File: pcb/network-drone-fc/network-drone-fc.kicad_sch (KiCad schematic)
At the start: 80 parts, among them J1 U.FL-R-SMT-1, J2 TYPE-C 16PIN 2MD, J3 U.FL GPS, J4 ESC, J5 Sensor port 5V I2C, J6 Radio UART 5V, J7 Charging board, U1 ESP32-S3FN8, U2 USBLC6-2SC6, U3 AP63205WU-7, U4 TLV75733PDRVR, U5 TPS7A2033PDBVR, U6 ICM-42688-P, U7 BMP581, U8 MAX-M10S, X1 Q22FA12800101

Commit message: Schematic: C16 footprint field set to 1206 to match the board
The board has carried the 1206 since the capacitor was enlarged; the schematic's footprint field still named the 0805. No copper change.
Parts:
- C16: footprint Capacitor_SMD:C_0805_2012Metric -> Capacitor_SMD:C_1206_3216Metric
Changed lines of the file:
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@@
 			)
 		)
-		(property "Footprint" "Capacitor_SMD:C_0805_2012Metric"
+		(property "Footprint" "Capacitor_SMD:C_1206_3216Metric"
 			(at 138.1252 50.8 0)
 			(effects

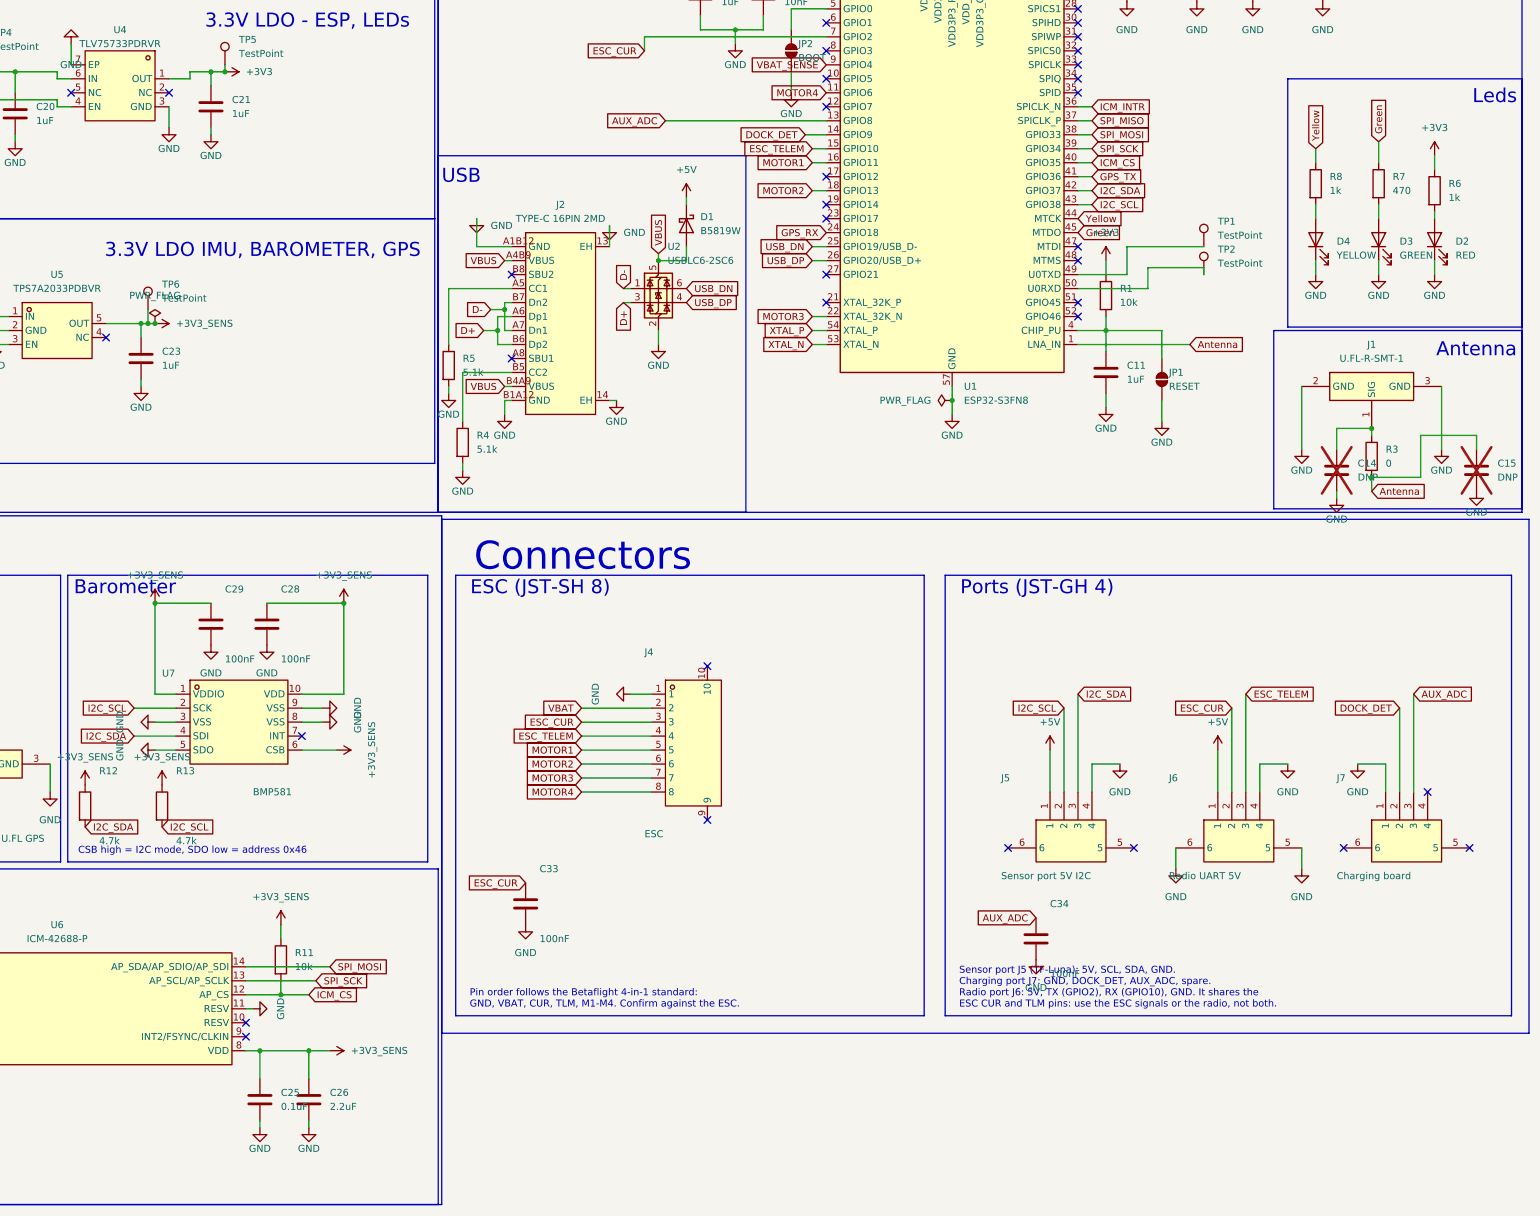
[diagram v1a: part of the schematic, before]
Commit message: Schematic: charging port J7 grows to 7 pins (battery, GND, I2C, power good, charge status, charge disable); landing sensor port J8 added; I2C pull-ups to 2.2k
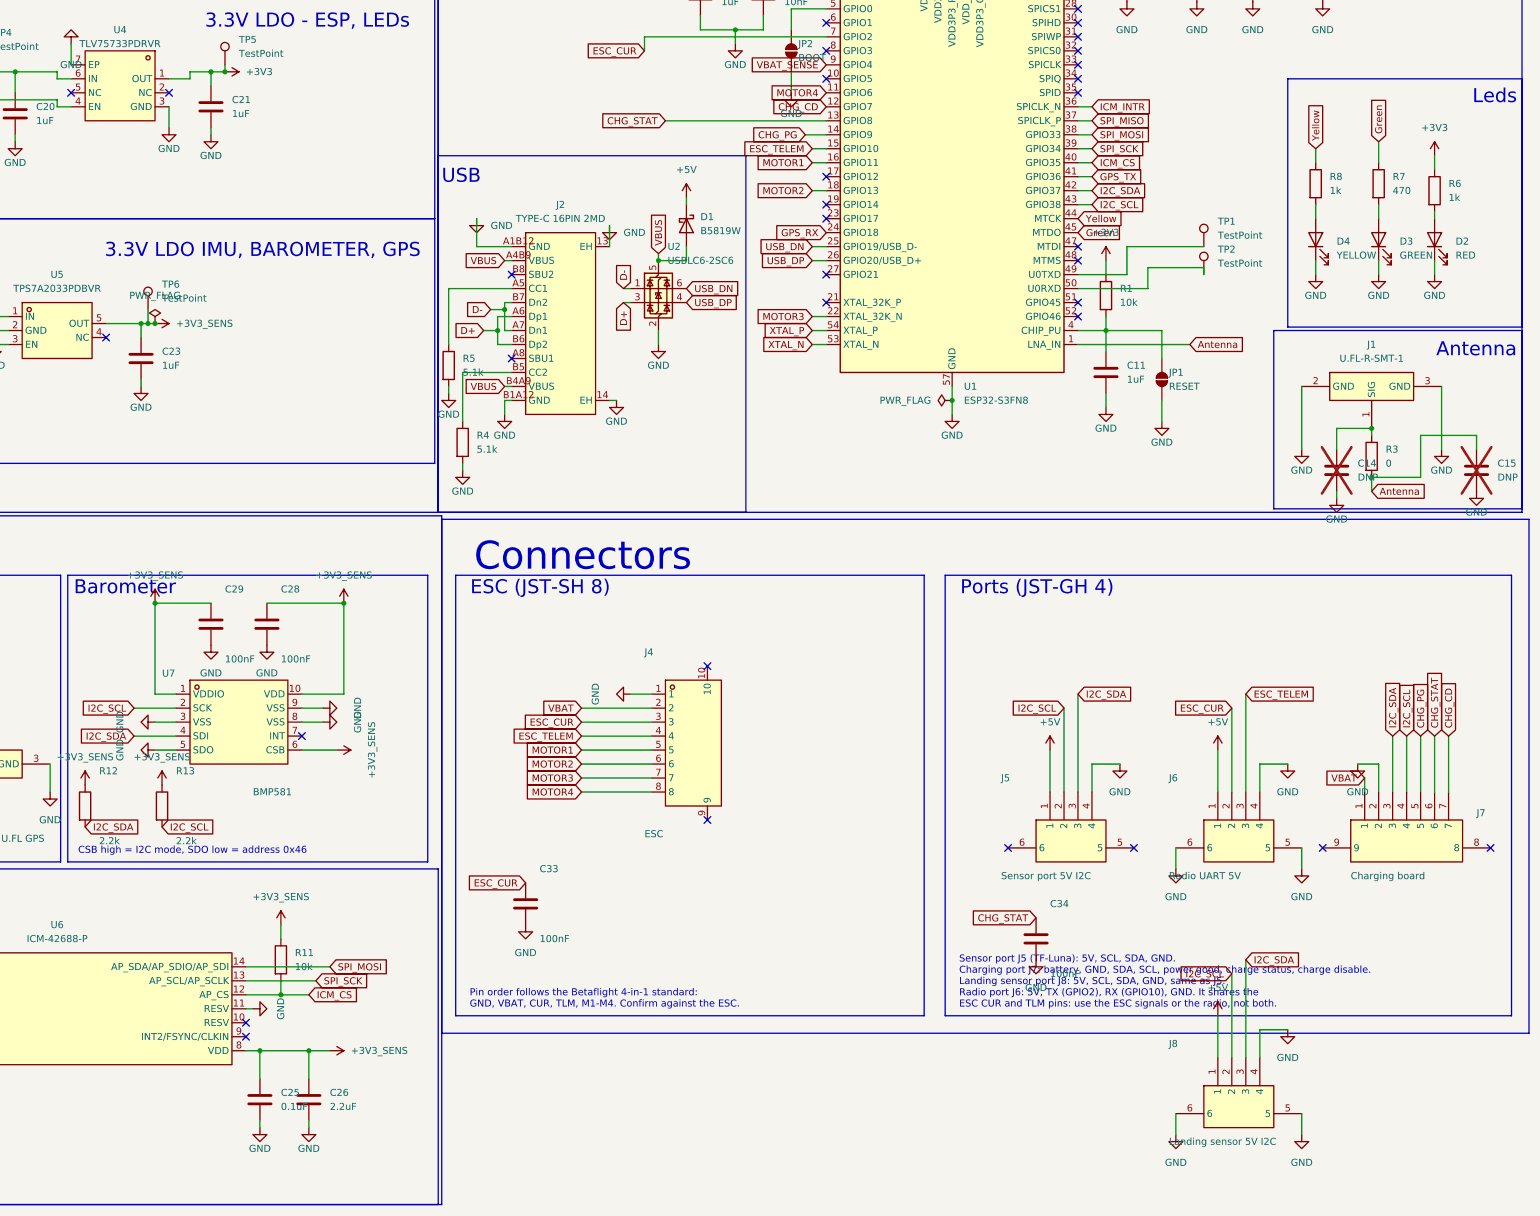
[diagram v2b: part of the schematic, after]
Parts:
- added J8: Landing sensor 5V I2C, tar_fc:JST_SH_BM04B-SRSS-TB_1x04_Vertical, symbol tar_fc:SM04B-GHS-TB
- J7: footprint tar_fc:CONN-SMD_4P-P1.25_SM04B-GHS-TB-LF-SN -> tar_fc:JST_SH_SM07B-SRSS-TB_1x07_Horizontal; symbol tar_fc:SM04B-GHS-TB -> tar_fc:SM07B-SRSS-TB; LCSC C189895 -> (none)
- R12, R13: value 4.7k -> 2.2k
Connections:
- net +5V: now also J8.1
- net GND: now also J7.2, J8.4, J8.5, J8.6; no longer J7.1
- net I2C_SCL: now also J7.4, J8.2
- net I2C_SDA: now also J7.3, J8.3
- net VBAT: now also J7.1
- net CHG_CD: now reaches U1.12 (GPIO7)
- net CHG_CD: now also J7.7
- net CHG_PG: now reaches J7.5
- net CHG_PG: now also U1.14 (GPIO9)
- net CHG_STAT: now reaches J7.6
- net CHG_STAT: now also C34.1, U1.13 (GPIO8)
- removed net AUX_ADC: C34.1, J7.3, U1.13 (GPIO8)
- removed net DOCK_DET: J7.2, U1.14 (GPIO9)
- no-connect marks 46 -> 44
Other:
- note added: "Sensor port J5 (TF-Luna): 5V, SCL, SDA, GND. Charging port J7: battery, GND, SDA, SCL, power good, charge status, charge disable. Landing sensor port J8: 5V, SCL, SDA, GND, same as J5. Radio port J6: 5V, TX (GPIO2), RX (GPIO10), GND. It shares the ESC CUR and TLM pins: use the ESC signals or the radio, not both."
- note removed: "Sensor port J5 (TF-Luna): 5V, SCL, SDA, GND. Charging port J7: GND, DOCK_DET, AUX_ADC, spare. Radio port J6: 5V, TX (GPIO2), RX (GPIO10), GND. It shares the ESC CUR and TLM pins: use the ESC signals or the radio, not both."

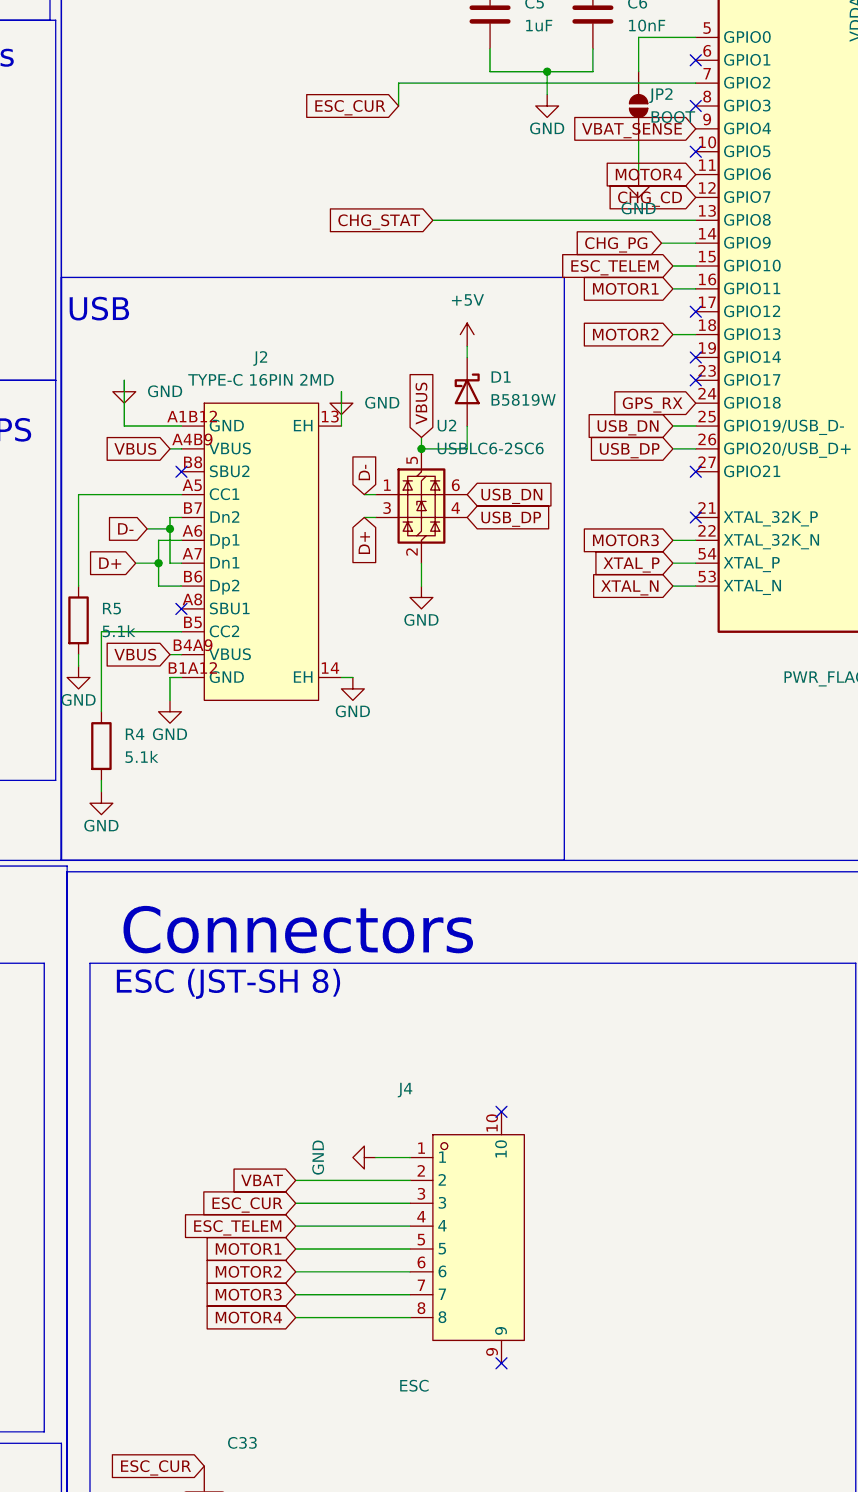
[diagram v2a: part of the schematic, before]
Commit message: Schematic: J4 relabelled to the ESC's pin order (GND, VBAT, motors 1 to 4, N, C), motor numbers moved between GPIOs
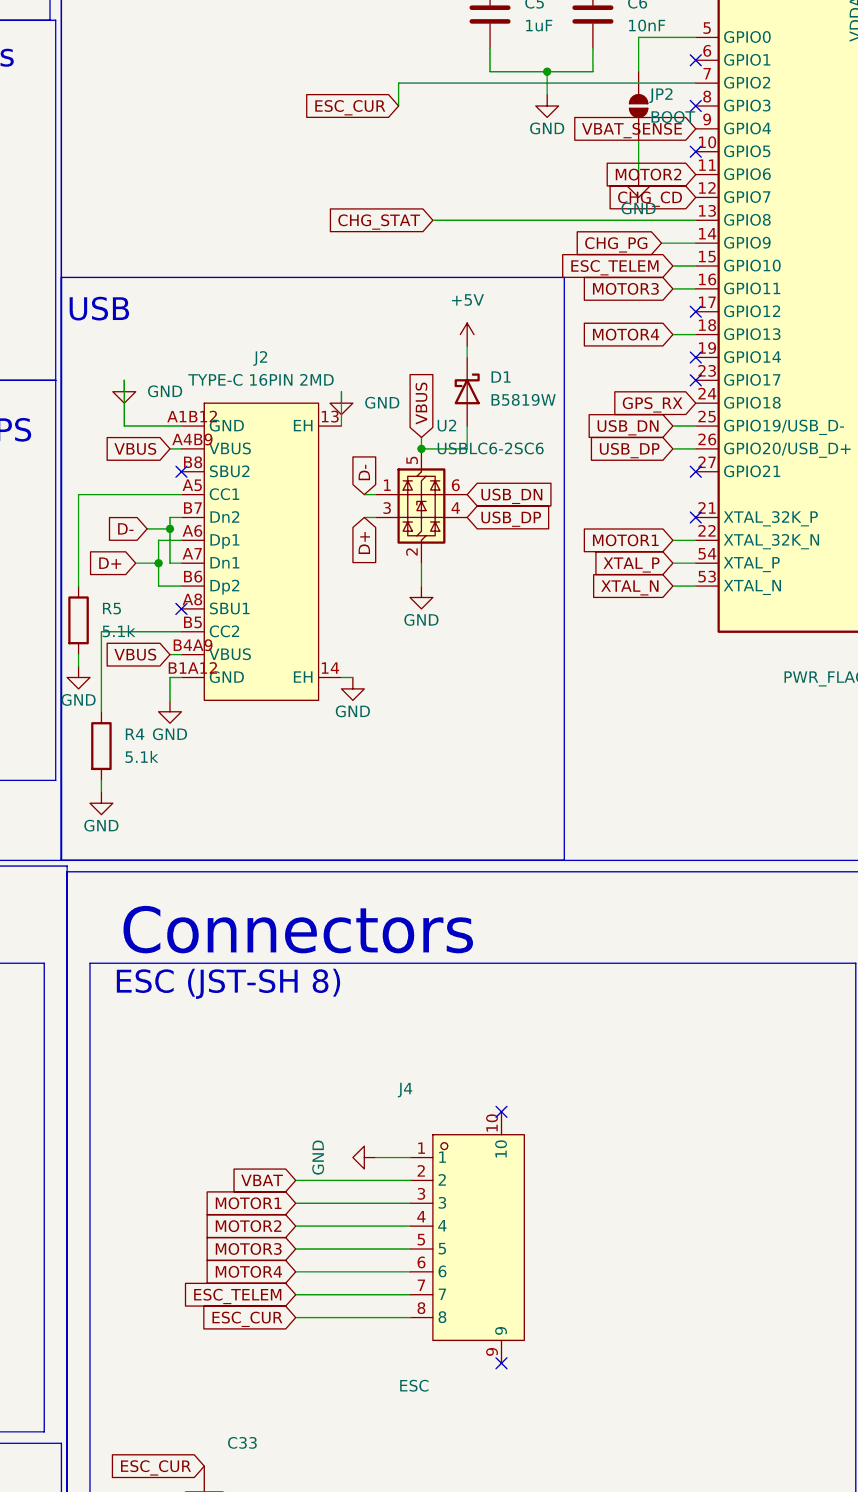
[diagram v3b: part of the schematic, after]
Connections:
- net ESC_CUR: now also J4.8; no longer J4.3
- net ESC_TELEM: now also J4.7; no longer J4.4
- net MOTOR1: now also J4.3, U1.22 (XTAL_32K_N); no longer J4.5, U1.16 (GPIO11)
- net MOTOR2: now also J4.4, U1.11 (GPIO6); no longer J4.6, U1.18 (GPIO13)
- net MOTOR3: now also J4.5, U1.16 (GPIO11); no longer J4.7, U1.22 (XTAL_32K_N)
- net MOTOR4: now also J4.6, U1.18 (GPIO13); no longer J4.8, U1.11 (GPIO6)
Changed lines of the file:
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@@
 		)
 	)
-	(global_label "MOTOR2"
+	(global_label "MOTOR4"
 		(shape input)
 		(at 278.13 100.33 180)
@@
 		)
 	)
-	(global_label "MOTOR1"
+	(global_label "MOTOR3"
 		(shape input)
 		(at 278.13 95.25 180)
@@
 		)
 	)
-	(global_label "ESC_CUR"
+	(global_label "MOTOR1"
 		(shape input)
 		(at 236.22 196.85 180)
@@
 		)
 	)
-	(global_label "ESC_TELEM"
+	(global_label "MOTOR2"
 		(shape input)
 		(at 236.22 199.39 180)
@@
 		)
 	)
-	(global_label "MOTOR1"
+	(global_label "MOTOR3"
 		(shape input)
 		(at 236.22 201.93 180)
@@
 		)
 	)
-	(global_label "MOTOR2"
+	(global_label "MOTOR4"
 		(shape input)
 		(at 236.22 204.47 180)
@@
 		)
 	)
-	(global_label "MOTOR3"
+	(global_label "ESC_TELEM"
 		(shape input)
 		(at 236.22 207.01 180)
@@
 		)
 	)
-	(global_label "MOTOR4"
+	(global_label "ESC_CUR"
 		(shape input)
 		(at 236.22 209.55 180)
@@
 		)
 	)
-	(global_label "MOTOR3"
+	(global_label "MOTOR1"
 		(shape input)
 		(at 278.13 123.19 180)
@@
 		)
 	)
-	(global_label "MOTOR4"
+	(global_label "MOTOR2"
 		(shape input)
 		(at 280.67 82.55 180)

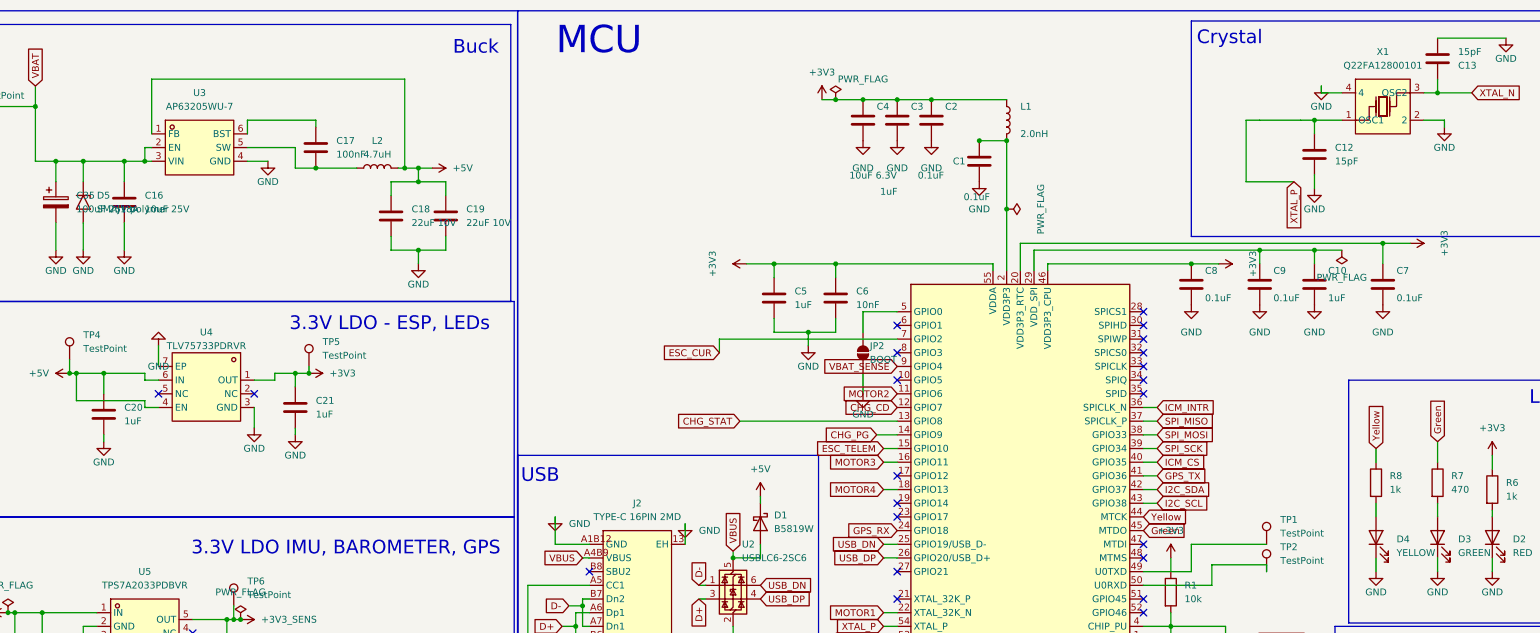
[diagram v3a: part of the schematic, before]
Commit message: Part values: SMAJ12A surge diode, 16 V buck output capacitors, crystal and diode labels match the parts ordered
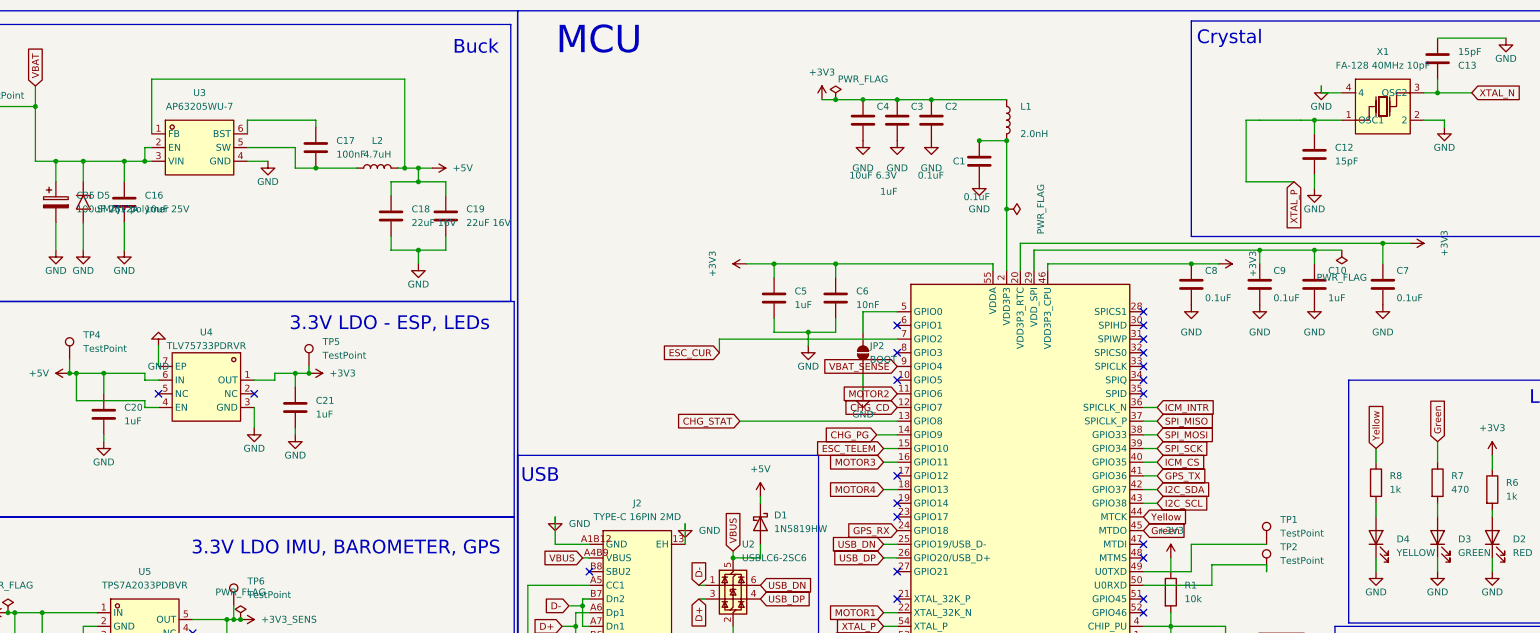
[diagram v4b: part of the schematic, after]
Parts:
- C18, C19: value 22uF 10V -> 22uF 16V
- D1: value B5819W -> 1N5819HW
- D5: value SMAJ18A -> SMAJ12A
- X1: value Q22FA12800101 -> FA-128 40MHz 10pF
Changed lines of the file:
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@@
 			)
 		)
-		(property "Value" "B5819W"
+		(property "Value" "1N5819HW"
 			(at 257.81 107.6324 90)
 			(effects
@@
 			)
 		)
-		(property "Value" "22uF 10V"
+		(property "Value" "22uF 16V"
 			(at 200.66 50.7999 0)
 			(effects
@@
 			)
 		)
-		(property "Value" "SMAJ18A"
+		(property "Value" "SMAJ12A"
 			(at 132.08 48.2599 90)
 			(effects
@@
 			)
 		)
-		(property "Value" "22uF 10V"
+		(property "Value" "22uF 16V"
 			(at 190.5 50.7999 0)
 			(effects
@@
 			)
 		)
-		(property "Value" "Q22FA12800101"
+		(property "Value" "FA-128 40MHz 10pF"
 			(at 370.84 21.59 0)
 			(effects

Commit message: Schematic: 100 nF on VBUS at the USB protection chip, 10k pull-up on the boot pin (net BOOT)
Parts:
- added C36: 100nF, Capacitor_SMD:C_0402_1005Metric, symbol Device:C
- added R16: 10k, Resistor_SMD:R_0402_1005Metric, symbol Device:R
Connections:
- net +3V3: now also R16.1
- net GND: now also C36.2
- net VBUS: now also C36.1
- net BOOT: now reaches JP2.2 (B), U1.5 (GPIO0)
- net BOOT: now also R16.2

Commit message: Battery cut-off on the 5 V regulator's enable pin
R14 143k and R15 34k on the bottom set the AP63205 to turn on at about
5.9 V and off at about 4.9 V. C16 is now 0805 so the battery reaches VIN
through its own channel, and the green LED track moves left under the
regulator to make room for the enable via.
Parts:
- added R14: 143k, Resistor_SMD:R_0402_1005Metric, symbol Device:R
- added R15: 34k, Resistor_SMD:R_0402_1005Metric, symbol Device:R
- C16: footprint Capacitor_SMD:C_1206_3216Metric -> Capacitor_SMD:C_0805_2012Metric
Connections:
- net GND: now also R15.2
- net VBAT: now also R14.1; no longer U3.2 (EN)
- new net BUCK_EN: R14.2, R15.1, U3.2 (EN)
